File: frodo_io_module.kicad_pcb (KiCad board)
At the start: 4 copper layers, 60 x 60 mm, 162 parts, among them J1 Conn_02x04_Top_Bottom, J10 JST-GH 4Pin, J11 JST-GH 4Pin, J14 Conn_02x03_Odd_Even, J16 USB_C_Receptacle_USB2.0, J17 TC2050, J2 Conn_02x10_Odd_Even, J3 Conn_02x04_Top_Bottom, J4 Conn_02x03_Odd_Even, J6 JST-GH 4Pin, J7 JST-GH 4Pin, J8 JST-GH 4Pin, J9 JST-GH 4Pin, Q1 AOSP21321, Q2 AOSP21321, Q3 NMOS, Q4 NMOS, Q5 AOSP21321, Q6 AOSP21321, Q7 NMOS, Q8 NMOS, SW1 KMR721NGLFS, SW2 KMR721NGLFS, SW3 KMR721NGLFS, U1 L7805, U10 MCP2562-E-SN, U11 TPD4E1U06, U12 INA181A1, U2 L7805, U3 STM32F105RCTx, U5 AZ1117-3.3, U6 W25Q128JVP, U7 MCP2562-E-SN, U8 TPD4E1U06, U9 INA181A1, Y1 8MHz 12pF

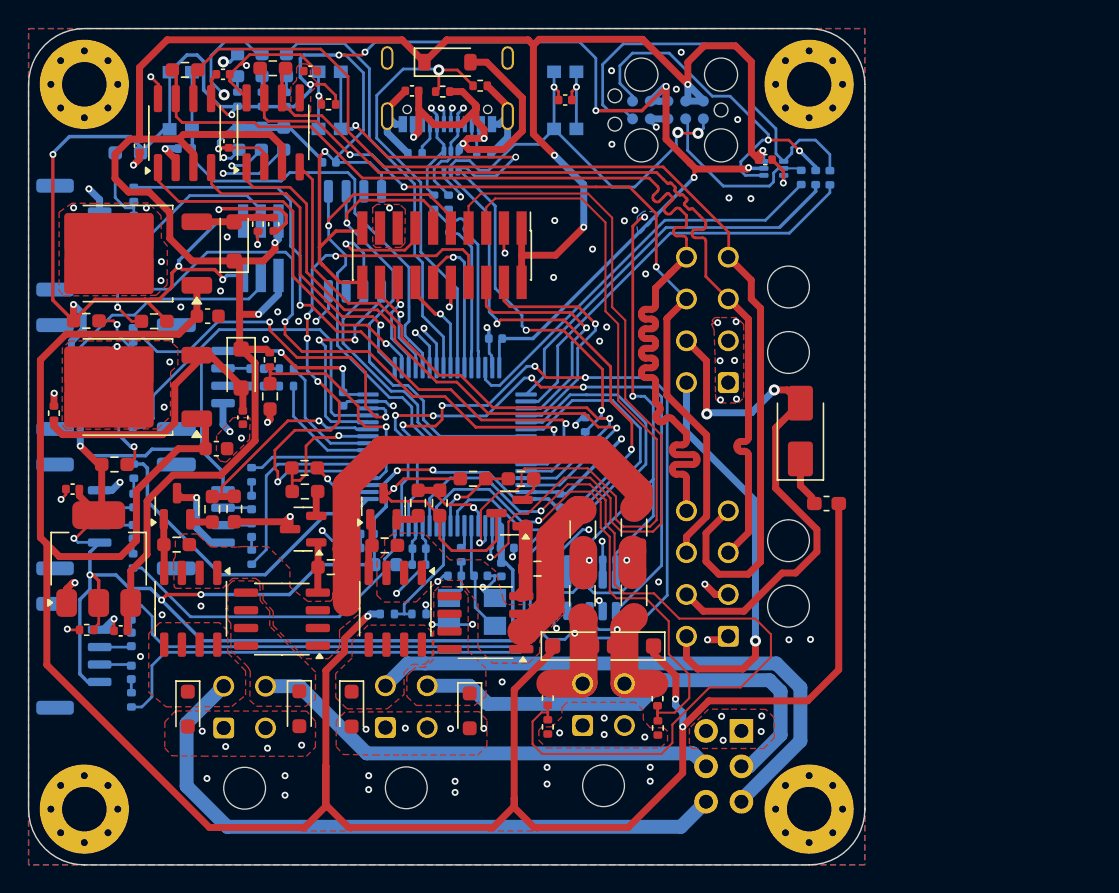
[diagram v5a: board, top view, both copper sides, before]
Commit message: started new design iteration, some scematic fixes (servo pwm&5v option, tsv issue)
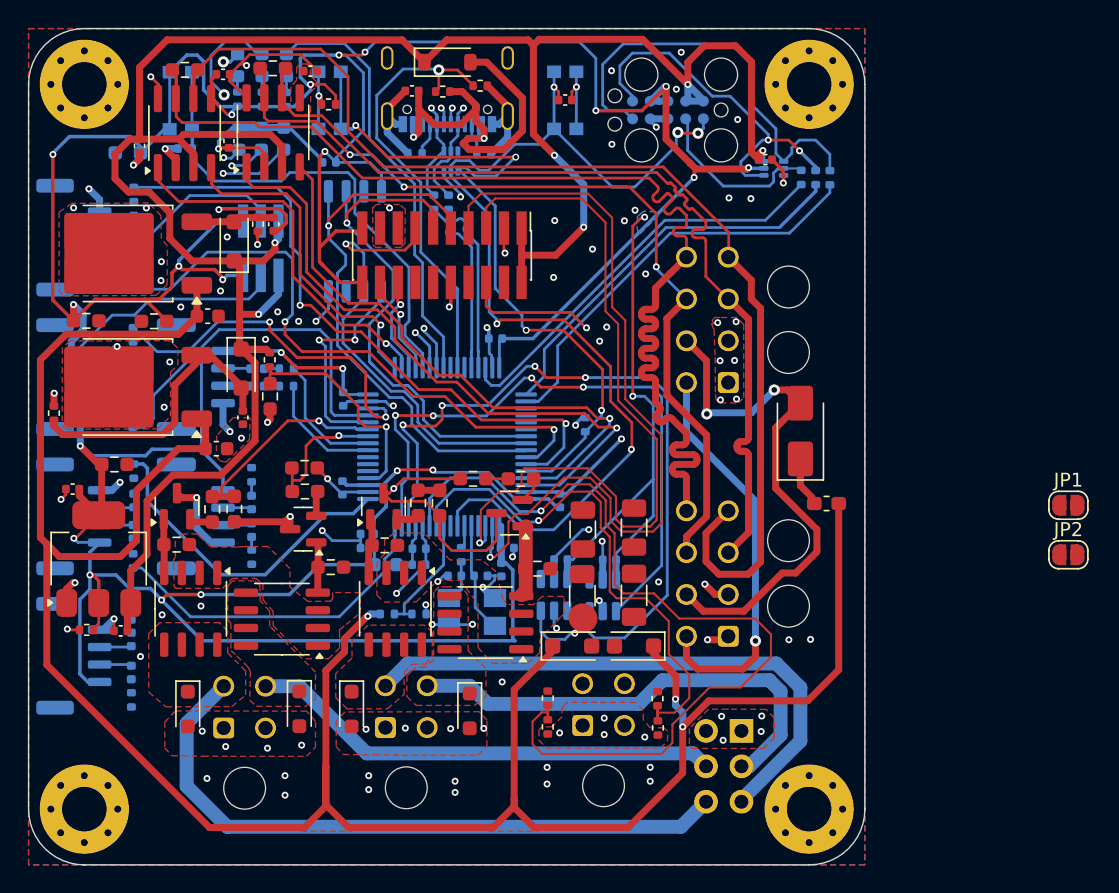
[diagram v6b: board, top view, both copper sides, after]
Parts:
- added JP1: SolderJumper_2_Open, Jumper:SolderJumper-2_P1.3mm_Open_RoundedPad1.0x1.5mm, F.Cu at (174.6, 134.2)
- added JP2: SolderJumper_2_Open, Jumper:SolderJumper-2_P1.3mm_Open_RoundedPad1.0x1.5mm, F.Cu at (174.6, 137.8)
- F2, F3: value 10A -> 5A
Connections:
- D13 pad 2: SH21 -> high_current2
- D14 pad 2: SH11 -> high_current
- F2 pad 1: /Digital Output/VD -> SH11
- F2 pad 2: SH12 -> high_current
- F3 pad 1: /Digital Output1/VD -> SH21
- F3 pad 2: SH22 -> high_current2
- J12 pad 3: SH11 -> high_current
- J12 pad 4: SH21 -> high_current2
- J2 pad 12: IO-8 -> IO-8 (ADC)
- J2 pad 14: IO-3 (ADC) -> IO-3
- J2 pad 8: IO-2 (ADC/DAC) -> IO-2
- Q1 pad 1: /Digital Output/VD -> SH12
- Q1 pad 2: /Digital Output/VD -> SH12
- Q1 pad 3: /Digital Output/VD -> SH12
- Q2 pad 1: /Digital Output/VD -> SH12
- Q2 pad 2: /Digital Output/VD -> SH12
- Q2 pad 3: /Digital Output/VD -> SH12
- Q5 pad 1: /Digital Output1/VD -> SH22
- Q5 pad 2: /Digital Output1/VD -> SH22
- Q5 pad 3: /Digital Output1/VD -> SH22
- Q6 pad 1: /Digital Output1/VD -> SH22
- Q6 pad 2: /Digital Output1/VD -> SH22
- Q6 pad 3: /Digital Output1/VD -> SH22
- R10 pad 2: Net-(FB3-Pad1) -> Net-(J7-Pin_2)
- R12 pad 2: Net-(FB5-Pad1) -> Net-(J6-Pin_3)
- R13 pad 2: Net-(FB6-Pad1) -> Net-(J7-Pin_3)
- R18 pad 2: Net-(FB8-Pad1) -> Net-(J9-Pin_2)
- R19 pad 2: Net-(FB9-Pad1) -> Net-(J10-Pin_2)
- R21 pad 2: Net-(FB11-Pad1) -> Net-(J9-Pin_3)
- R22 pad 2: Net-(FB12-Pad1) -> Net-(J10-Pin_3)
- R4 pad 2: Net-(FB2-Pad1) -> Net-(J6-Pin_2)
- R43 pad 1: SH11 -> high_current
- R44 pad 1: SH21 -> high_current2
- R5 pad 1: Net-(FB5-Pad1) -> Net-(J6-Pin_3)
- R52 pad 1: /Digital Output/VD -> SH12
- R53 pad 1: /Digital Output/VD -> SH12
- R58 pad 1: /Digital Output1/VD -> SH22
- R59 pad 1: /Digital Output1/VD -> SH22
- R6 pad 2: Net-(FB8-Pad1) -> Net-(J9-Pin_2)
- R7 pad 1: Net-(FB11-Pad1) -> Net-(J9-Pin_3)
- R9 pad 2: Net-(FB2-Pad1) -> Net-(J6-Pin_2)
- U3 pad 21: IO-2 (ADC/DAC) -> AIN1
- U3 pad 22: AIN1 -> AIN0
- U3 pad 23: AIN0 -> HC_OUT_1
- U3 pad 4: HC_OUT_2 -> IO-2
- U3 pad 41: IO-3 (ADC) -> HC_OUT_2
- U3 pad 43: IO-8 -> IO-3
- U3 pad 51: IO-0 (UART5 TX) -> COM4_1
- U3 pad 52: IO-1 (UART5 RX) -> COM4_2
- U3 pad 53: COM4_1 -> IO-0 (UART5 TX)
- U3 pad 54: COM4_2 -> IO-1 (UART5 RX)
- U3 pad 8: HC_OUT_1 -> IO-8 (ADC)
- U8 pad 6: /VBUS -> +5V
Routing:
- net COM4_1: track 62.4 -> 0.00 mm
- net COM4_2: track 60.0 -> 0.00 mm
- net IO-2 (ADC/DAC): track 40.6 -> 0.00 mm, vias 5 -> 0
- net /Digital Output1/VD: track 33.0 -> 0.00 mm
- net IO-1 (UART5 RX): track 17.9 -> 0.00 mm, vias 1 -> 0
- net AIN1: track 14.4 -> 0.00 mm
- net /Digital Output/VD: track 10.9 -> 0.00 mm
- net IO-8: track 10.4 -> 0.00 mm, vias 1 -> 0
- net SH21: track 10.1 -> 0.00 mm, vias 1 -> 0
- net AIN0: track 8.66 -> 0.00 mm
- net IO-0 (UART5 TX): track 18.0 -> 9.83 mm
- net SH12: track 7.73 -> 0.00 mm, vias 1 -> 0
- net SH22: track 7.40 -> 0.00 mm, vias 1 -> 0
- net SH11: track 11.5 -> 4.48 mm
- net IO-3 (ADC): track 6.54 -> 0.00 mm, vias 1 -> 0
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- added copper zone on F.Cu, net SH12
- added copper zone on F.Cu, net SH22
- removed copper zone on F.Cu, net /Digital Output/VD
- removed copper zone on F.Cu, net /Digital Output1/VD
